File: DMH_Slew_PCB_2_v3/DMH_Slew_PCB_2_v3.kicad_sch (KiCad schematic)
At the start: 0 parts

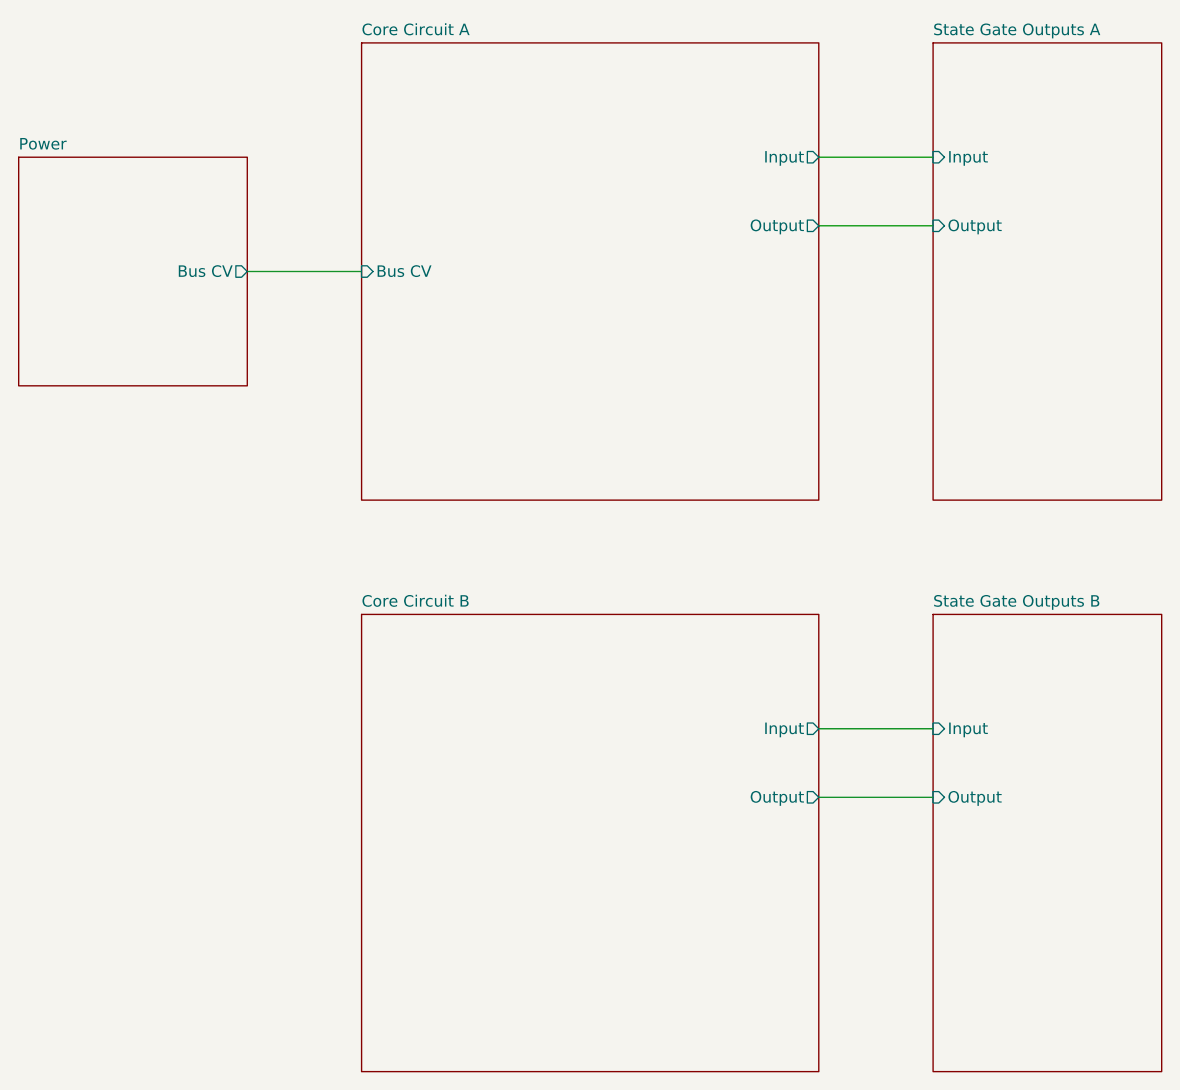
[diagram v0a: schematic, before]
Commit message: Relinked PCB1 and 2 with new v3 schematics
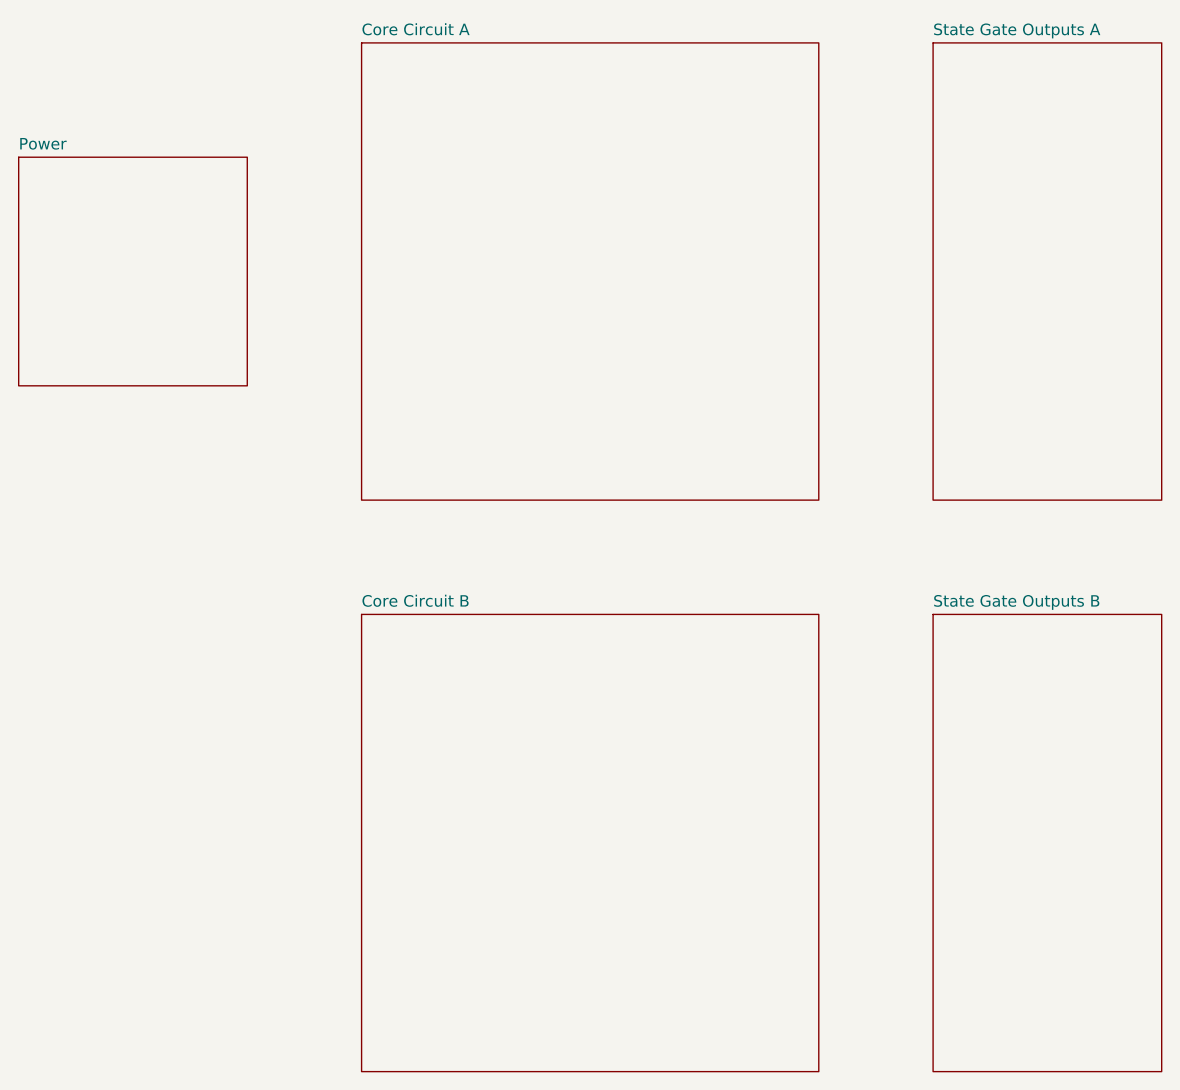
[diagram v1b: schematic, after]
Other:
- sheet Core Circuit A ports: added none; removed Bus CV, Input, Output
- sheet Core Circuit B ports: added none; removed Input, Output
- sheet Power ports: added none; removed Bus CV
- sheet State Gate Outputs A ports: added none; removed Input, Output
- sheet State Gate Outputs B ports: added none; removed Input, Output
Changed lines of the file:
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@@
 		(comment 1 "PCB for 5 cm Kosmo format synthesizer module")
-	)
-	(wire
-		(pts
-			(xy 114.3 45.72) (xy 127 45.72)
-		)
-		(stroke
-			(width 0)
-			(type default)
-		)
-	)
-	(wire
-		(pts
-			(xy 114.3 38.1) (xy 127 38.1)
-		)
-		(stroke
-			(width 0)
-			(type default)
-		)
-	)
-	(wire
-		(pts
-			(xy 114.3 101.6) (xy 127 101.6)
-		)
-		(stroke
-			(width 0)
-			(type default)
-		)
-	)
-	(wire
-		(pts
-			(xy 50.8 50.8) (xy 63.5 50.8)
-		)
-		(stroke
-			(width 0)
-			(type default)
-		)
-	)
-	(wire
-		(pts
-			(xy 114.3 109.22) (xy 127 109.22)
-		)
-		(stroke
-			(width 0)
-			(type default)
-		)
 	)
 	(sheet
@@
 			)
 		)
-		(pin "Bus CV" output
-			(at 50.8 50.8 0)
-			(effects
-				(font
-					(size 1.27 1.27)
-				)
-				(justify right)
-			)
-		)
-		(instances
-			(project "DMH_Slew_PCB_2_v2"
+		(instances
+			(project "DMH_Slew_PCB_2_v3"
 				(path "/58f4306d-5387-4983-bb08-41a2313fd315"
 					(page "6")
@@
 			)
 		)
-		(pin "Input" input
-			(at 127 38.1 180)
-			(effects
-				(font
-					(size 1.27 1.27)
-				)
-				(justify left)
-			)
-		)
-		(pin "Output" input
-			(at 127 45.72 180)
-			(effects
-				(font
-					(size 1.27 1.27)
-				)
-				(justify left)
-			)
-		)
-		(instances
-			(project "DMH_Slew_PCB_2_v2"
+		(instances
+			(project "DMH_Slew_PCB_2_v3"
 				(path "/58f4306d-5387-4983-bb08-41a2313fd315"
 					(page "3")
@@
 			)
 		)
-		(pin "Input" output
-			(at 114.3 101.6 0)
-			(effects
-				(font
-					(size 1.27 1.27)
-				)
-				(justify right)
-			)
-		)
-		(pin "Output" output
-			(at 114.3 109.22 0)
-			(effects
-				(font
-					(size 1.27 1.27)
-				)
-				(justify right)
-			)
-		)
-		(instances
-			(project "DMH_Slew_PCB_2_v2"
+		(instances
+			(project "DMH_Slew_PCB_2_v3"
 				(path "/58f4306d-5387-4983-bb08-41a2313fd315"
 					(page "4")
@@
 			)
 		)
-		(pin "Input" output
-			(at 114.3 38.1 0)
-			(effects
-				(font
-					(size 1.27 1.27)
-				)
-				(justify right)
-			)
-		)
-		(pin "Output" output
-			(at 114.3 45.72 0)
-			(effects
-				(font
-					(size 1.27 1.27)
-				)
-				(justify right)
-			)
-		)
-		(pin "Bus CV" input
-			(at 63.5 50.8 180)
-			(effects
-				(font
-					(size 1.27 1.27)
-				)
-				(justify left)
-			)
-		)
-		(instances
-			(project "DMH_Slew_PCB_2_v2"
+		(instances
+			(project "DMH_Slew_PCB_2_v3"
 				(path "/58f4306d-5387-4983-bb08-41a2313fd315"
 					(page "2")
@@
 			)
 		)
-		(pin "Input" input
-			(at 127 101.6 180)
-			(effects
-				(font
-					(size 1.27 1.27)
-				)
-				(justify left)
-			)
-		)
-		(pin "Output" input
-			(at 127 109.22 180)
-			(effects
-				(font
-					(size 1.27 1.27)
-				)
-				(justify left)
-			)
-		)
-		(instances
-			(project "DMH_Slew_PCB_2_v2"
+		(instances
+			(project "DMH_Slew_PCB_2_v3"
 				(path "/58f4306d-5387-4983-bb08-41a2313fd315"
 					(page "5")
